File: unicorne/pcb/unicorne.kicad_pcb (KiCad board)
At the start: 2 copper layers, 133.8 x 91.4 mm, 98 parts, among them J3 LED, P1 i2c-pin, P2 i2c-pin, SW1 SW_PUSH, SW10 SW_PUSH, SW11 SW_PUSH, SW12 SW_PUSH, SW13 SW_PUSH, SW14 SW_PUSH, SW15 SW_PUSH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

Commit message: seems functional but I haven't done a thorough test
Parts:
- G***: footprint kbd:corne -> kbd:unicorne_silktext
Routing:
- added copper zone on B.Cu, net GND
- added copper zone on F.Cu, net GND

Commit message: corrected silk text
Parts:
- G***: footprint kbd:corne -> kbd:unicorne_silktext
- moved G*** 3.58 mm to (183.1, 82.0)
- moved G*** 1.69 mm to (185.5, 85.9)
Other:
- board text added: "Unicorne Chocolate v0.1"
- board text removed: "Corne Chocolate v2.1 PCB designed by foostan"

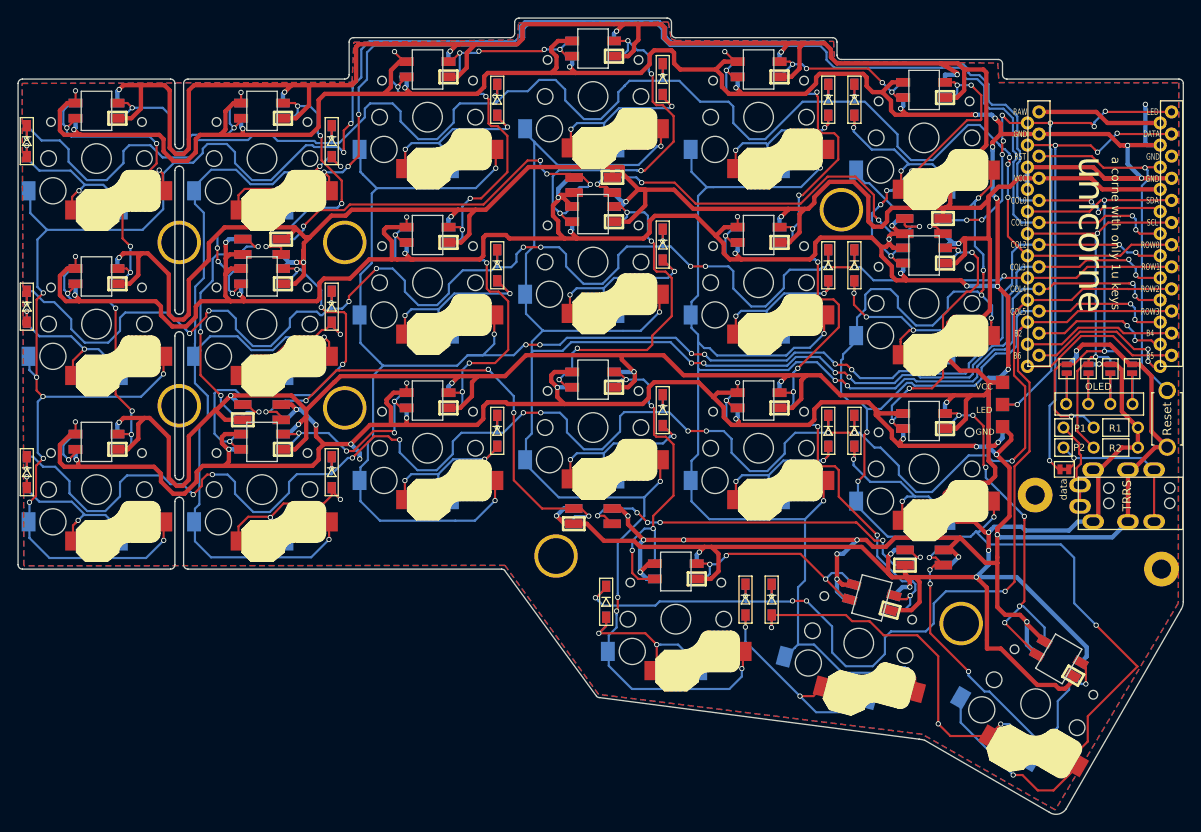
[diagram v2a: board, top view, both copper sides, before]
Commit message: trying to sort out git asking for credentials: modified the .git/config file so that it uses SSH, not sure if this will work
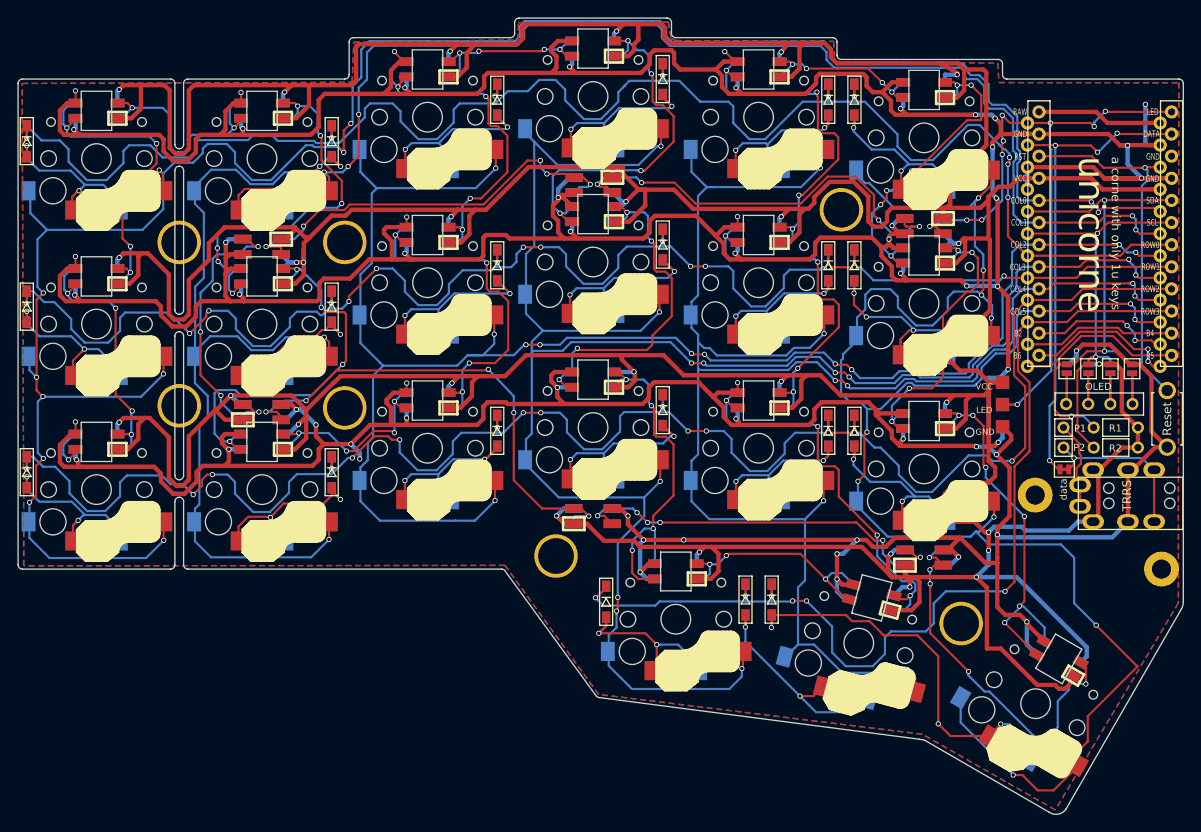
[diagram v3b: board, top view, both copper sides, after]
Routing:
- net (no net): vias 1 -> 0
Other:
- outline, holes or cut-outs redrawn
